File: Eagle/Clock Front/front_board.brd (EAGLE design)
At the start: 9 parts

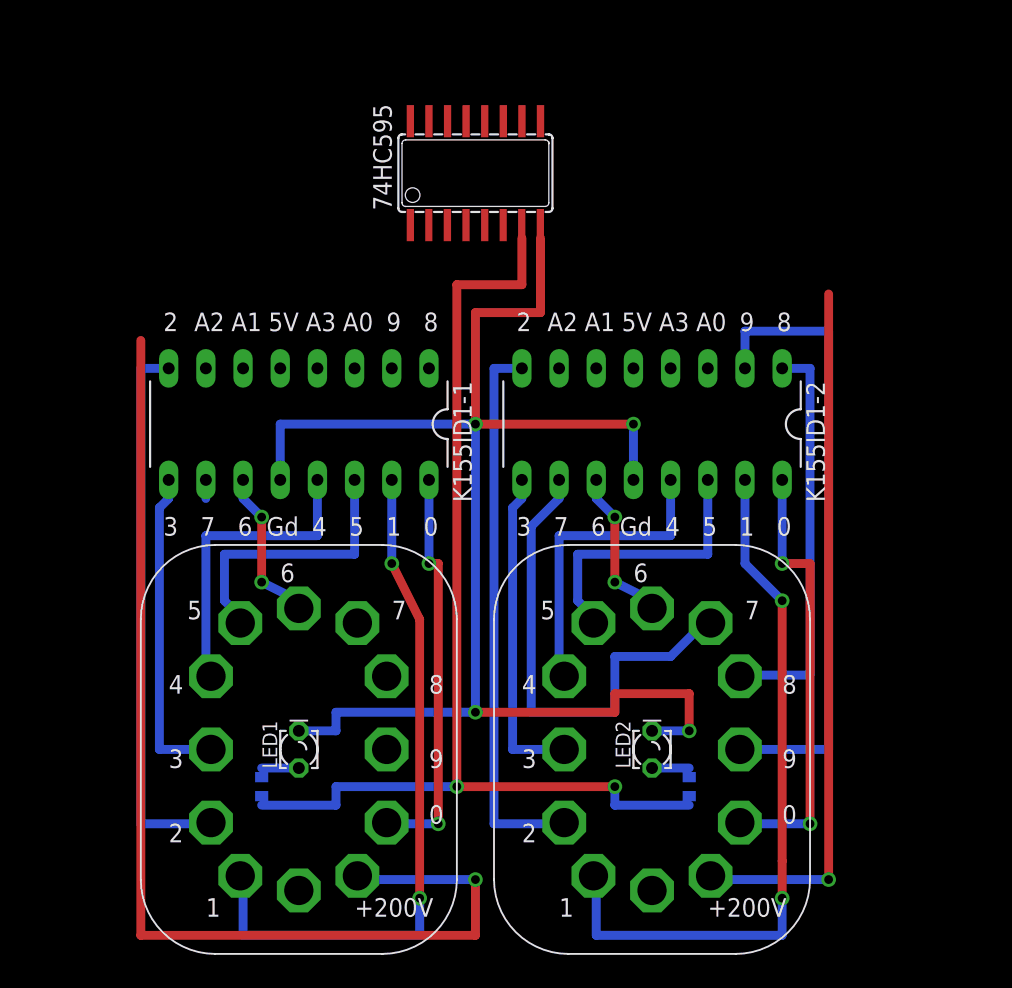
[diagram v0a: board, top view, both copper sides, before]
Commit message: Обновление печатной платы для цоколей
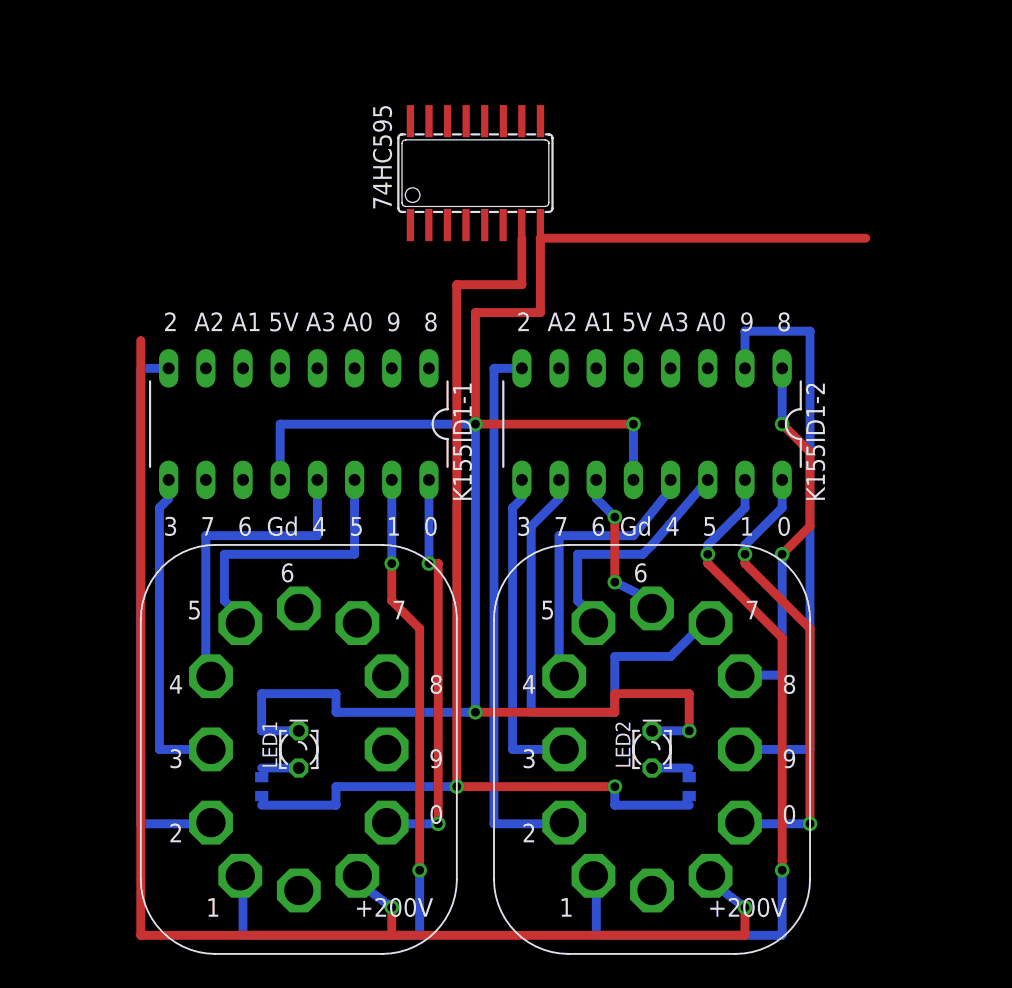
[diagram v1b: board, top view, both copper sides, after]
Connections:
- removed net S$20: K155ID1-1.11
- removed net S$9: K155ID1-1.10
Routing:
- net +200V1: track 75.6 -> 0.00 mm, vias 1 -> 0
- net +200V: track 48.3 -> 92.1 mm, vias 1 -> 2
- net GND: track 102.9 -> 132.7 mm
- net S$20: track 10.4 -> 0.00 mm, vias 2 -> 0
- net S$7: track 18.9 -> 16.2 mm
- net S$2: track 42.5 -> 40.0 mm
- net S$1: track 27.3 -> 25.1 mm, vias 0 -> 2
- net S$12: track 27.1 -> 29.2 mm
- net S$6: track 21.0 -> 19.3 mm
- net S$9: track 1.27 -> 0.00 mm
- net S$3: track 29.8 -> 30.8 mm
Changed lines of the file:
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@@
 <signals>
 <signal name="S$1">
-<wire x1="18.415" y1="-7.62" x2="22.86" y2="-7.62" width="0.6096" layer="16"/>
-<wire x1="22.86" y1="-7.62" x2="22.86" y2="13.335" width="0.6096" layer="16"/>
+<wire x1="18.415" y1="-7.62" x2="20.955" y2="-7.62" width="0.6096" layer="16"/>
+<wire x1="20.955" y1="-7.62" x2="20.955" y2="0.635" width="0.6096" layer="16"/>
+<wire x1="20.955" y1="0.635" x2="22.86" y2="2.54" width="0.6096" layer="1"/>
+<wire x1="22.86" y1="2.54" x2="22.86" y2="7.62" width="0.6096" layer="1"/>
+<wire x1="22.86" y1="7.62" x2="20.955" y2="9.525" width="0.6096" layer="1"/>
 <contactref element="K155ID1-2" pad="1"/>
-<wire x1="22.86" y1="13.335" x2="20.955" y2="13.335" width="0.6096" layer="16"/>
+<wire x1="20.955" y1="9.525" x2="20.955" y2="13.335" width="0.6096" layer="16"/>
+<via x="20.955" y="0.635" extent="1-16" drill="0.6" shape="square"/>
+<via x="20.955" y="9.525" extent="1-16" drill="0.6" shape="square"/>
 </signal>
 <signal name="S$2">
-<wire x1="18.415" y1="-12.7" x2="24.13" y2="-12.7" width="0.6096" layer="16"/>
-<wire x1="24.13" y1="-12.7" x2="24.13" y2="15.875" width="0.6096" layer="16"/>
-<wire x1="24.13" y1="15.875" x2="18.415" y2="15.875" width="0.6096" layer="16"/>
+<wire x1="18.415" y1="-12.7" x2="22.86" y2="-12.7" width="0.6096" layer="16"/>
+<wire x1="22.86" y1="-12.7" x2="22.86" y2="15.875" width="0.6096" layer="16"/>
+<wire x1="22.86" y1="15.875" x2="18.415" y2="15.875" width="0.6096" layer="16"/>
 <contactref element="K155ID1-2" pad="2"/>
 <wire x1="18.415" y1="15.875" x2="18.415" y2="13.335" width="0.6096" layer="16"/>
@@
 <signal name="S$3">
 <wire x1="18.415" y1="-17.78" x2="22.86" y2="-17.78" width="0.6096" layer="16"/>
-<wire x1="22.86" y1="-17.78" x2="22.86" y2="0" width="0.6096" layer="1"/>
-<wire x1="22.86" y1="0" x2="20.955" y2="0" width="0.6096" layer="1"/>
+<wire x1="22.86" y1="-17.78" x2="22.86" y2="-4.445" width="0.6096" layer="1"/>
+<wire x1="22.86" y1="-4.445" x2="18.415" y2="0" width="0.6096" layer="1"/>
+<wire x1="18.415" y1="0" x2="18.415" y2="0.635" width="0.6096" layer="1"/>
 <contactref element="K155ID1-2" pad="16"/>
-<wire x1="20.955" y1="0" x2="20.955" y2="5.715" width="0.6096" layer="16"/>
-<via x="20.955" y="0" extent="1-16" drill="0.6" shape="square"/>
+<wire x1="18.415" y1="0.635" x2="18.415" y2="1.27" width="0.6096" layer="16"/>
+<wire x1="18.415" y1="1.27" x2="20.955" y2="3.81" width="0.6096" layer="16"/>
+<wire x1="20.955" y1="3.81" x2="20.955" y2="5.715" width="0.6096" layer="16"/>
+<via x="18.415" y="0.635" extent="1-16" drill="0.6" shape="square"/>
 <via x="22.86" y="-17.78" extent="1-16" drill="0.6" shape="square"/>
 </signal>
@@
 <signal name="S$6">
 <wire x1="5.715" y1="-7.62" x2="5.715" y2="1.905" width="0.6096" layer="16"/>
-<wire x1="5.715" y1="1.905" x2="13.335" y2="1.905" width="0.6096" layer="16"/>
+<wire x1="5.715" y1="1.905" x2="10.795" y2="1.905" width="0.6096" layer="16"/>
 <contactref element="K155ID1-2" pad="13"/>
-<wire x1="13.335" y1="1.905" x2="13.335" y2="5.715" width="0.6096" layer="16"/>
+<wire x1="10.795" y1="1.905" x2="13.335" y2="5.08" width="0.6096" layer="16"/>
+<wire x1="13.335" y1="5.08" x2="13.335" y2="5.715" width="0.6096" layer="16"/>
 </signal>
 <signal name="S$7">
 <wire x1="8.255" y1="-3.81" x2="6.985" y2="-2.54" width="0.6096" layer="16"/>
 <wire x1="6.985" y1="-2.54" x2="6.985" y2="0.635" width="0.6096" layer="16"/>
-<wire x1="6.985" y1="0.635" x2="15.875" y2="0.635" width="0.6096" layer="16"/>
+<wire x1="6.985" y1="0.635" x2="11.43" y2="0.635" width="0.6096" layer="16"/>
 <contactref element="K155ID1-2" pad="14"/>
-<wire x1="15.875" y1="0.635" x2="15.875" y2="5.715" width="0.6096" layer="16"/>
+<wire x1="11.43" y1="0.635" x2="12.065" y2="1.27" width="0.6096" layer="16"/>
+<wire x1="12.065" y1="1.27" x2="15.875" y2="5.715" width="0.6096" layer="16"/>
 </signal>
 <signal name="S$8">
@@
 </signal>
 <signal name="S$13">
-<wire x1="20.955" y1="-22.86" x2="20.955" y2="-20.32" width="0.6096" layer="1"/>
+<wire x1="20.955" y1="-20.955" x2="20.955" y2="-20.32" width="0.6096" layer="1"/>
 <wire x1="8.255" y1="-21.59" x2="8.255" y2="-25.4" width="0.6096" layer="16"/>
 <wire x1="8.255" y1="-25.4" x2="20.955" y2="-25.4" width="0.6096" layer="16"/>
-<wire x1="20.955" y1="-25.4" x2="20.955" y2="-22.86" width="0.6096" layer="16"/>
-<via x="20.955" y="-22.86" extent="1-16" drill="0.6" shape="square"/>
+<wire x1="20.955" y1="-25.4" x2="20.955" y2="-20.955" width="0.6096" layer="16"/>
+<via x="20.955" y="-20.955" extent="1-16" drill="0.6" shape="square"/>
 </signal>
 <signal name="S$12">
-<wire x1="20.955" y1="-20.32" x2="20.955" y2="-2.54" width="0.6096" layer="1"/>
-<wire x1="20.955" y1="-2.54" x2="18.415" y2="0" width="0.6096" layer="16"/>
+<wire x1="20.955" y1="-20.32" x2="20.955" y2="-5.08" width="0.6096" layer="1"/>
+<wire x1="20.955" y1="-5.08" x2="15.875" y2="0" width="0.6096" layer="1"/>
+<wire x1="15.875" y1="0" x2="15.875" y2="0.635" width="0.6096" layer="1"/>
 <contactref element="K155ID1-2" pad="15"/>
-<wire x1="18.415" y1="0" x2="18.415" y2="5.715" width="0.6096" layer="16"/>
-<via x="20.955" y="-2.54" extent="1-16" drill="0.6" shape="square"/>
+<wire x1="15.875" y1="0.635" x2="15.875" y2="1.27" width="0.6096" layer="16"/>
+<wire x1="15.875" y1="1.27" x2="18.415" y2="3.81" width="0.6096" layer="16"/>
+<wire x1="18.415" y1="3.81" x2="18.415" y2="5.715" width="0.6096" layer="16"/>
+<via x="15.875" y="0.635" extent="1-16" drill="0.6" shape="square"/>
 </signal>
 <signal name="S$11">
@@
 </signal>
 <signal name="+200V">
-<wire x1="15.875" y1="-21.59" x2="24.13" y2="-21.59" width="0.6096" layer="16"/>
-<via x="24.13" y="-21.59" extent="1-16" drill="0.6" shape="square"/>
-<wire x1="24.13" y1="-21.59" x2="24.13" y2="18.415" width="0.6096" layer="1"/>
+<wire x1="15.875" y1="-21.59" x2="18.415" y2="-23.495" width="0.6096" layer="16"/>
+<via x="18.415" y="-23.495" extent="1-16" drill="0.6" shape="square"/>
+<wire x1="18.415" y1="-23.495" x2="18.415" y2="-25.4" width="0.6096" layer="1"/>
+<wire x1="-8.255" y1="-21.59" x2="-5.715" y2="-23.495" width="0.6096" layer="16"/>
+<via x="-5.715" y="-23.495" extent="1-16" drill="0.6" shape="square"/>
+<wire x1="-5.715" y1="-23.495" x2="-5.715" y2="-25.4" width="0.6096" layer="1"/>
+<wire x1="-5.715" y1="-25.4" x2="-22.86" y2="-25.4" width="0.6096" layer="1"/>
+<wire x1="-22.86" y1="-25.4" x2="-22.86" y2="15.24" width="0.6096" layer="1"/>
+<wire x1="18.415" y1="-25.4" x2="-5.715" y2="-25.4" width="0.6096" layer="1"/>
 </signal>
 <signal name="S$14">
@@
 <wire x1="-8.255" y1="0.635" x2="-8.255" y2="5.715" width="0.6096" layer="16"/>
 </signal>
-<signal name="S$9">
-<contactref element="K155ID1-1" pad="10"/>
-<wire x1="-18.415" y1="4.445" x2="-18.415" y2="5.715" width="0.6096" layer="16"/>
-</signal>
-<signal name="S$20">
-<wire x1="-12.065" y1="-2.54" x2="-14.605" y2="-1.27" width="0.6096" layer="16"/>
-<contactref element="K155ID1-1" pad="11"/>
-<wire x1="-15.875" y1="4.445" x2="-15.875" y2="5.715" width="0.6096" layer="16"/>
-<wire x1="-14.605" y1="-1.27" x2="-14.605" y2="3.175" width="0.6096" layer="1"/>
-<wire x1="-14.605" y1="3.175" x2="-15.875" y2="4.445" width="0.6096" layer="16"/>
-<via x="-14.605" y="-1.27" extent="1-16" drill="0.6" shape="square"/>
-<via x="-14.605" y="3.175" extent="1-16" drill="0.6" shape="square"/>
-</signal>
 <signal name="S$22">
-<wire x1="-3.81" y1="-22.86" x2="-3.81" y2="-3.81" width="0.6096" layer="1"/>
-<wire x1="-3.81" y1="-3.81" x2="-5.715" y2="0" width="0.6096" layer="1"/>
+<wire x1="-3.81" y1="-20.955" x2="-3.81" y2="-4.445" width="0.6096" layer="1"/>
+<wire x1="-3.81" y1="-4.445" x2="-5.715" y2="-2.54" width="0.6096" layer="1"/>
+<wire x1="-5.715" y1="-2.54" x2="-5.715" y2="0" width="0.6096" layer="1"/>
 <contactref element="K155ID1-1" pad="15"/>
 <wire x1="-5.715" y1="0" x2="-5.715" y2="5.715" width="0.6096" layer="16"/>
@@
 <wire x1="-15.875" y1="-21.59" x2="-15.875" y2="-25.4" width="0.6096" layer="16"/>
 <wire x1="-15.875" y1="-25.4" x2="-3.81" y2="-25.4" width="0.6096" layer="16"/>
-<wire x1="-3.81" y1="-25.4" x2="-3.81" y2="-22.86" width="0.6096" layer="16"/>
-<via x="-3.81" y="-22.86" extent="1-16" drill="0.6" shape="square"/>
+<wire x1="-3.81" y1="-25.4" x2="-3.81" y2="-20.955" width="0.6096" layer="16"/>
+<via x="-3.81" y="-20.955" extent="1-16" drill="0.6" shape="square"/>
 </signal>
 <signal name="GND1">
 <wire x1="-22.86" y1="-15.24" x2="-22.86" y2="9.525" width="0" layer="19" extent="1-16"/>
 <wire x1="-22.86" y1="-15.24" x2="-24.13" y2="-15.24" width="0" layer="19" extent="1-16"/>
-</signal>
-<signal name="+200V1">
-<wire x1="-8.255" y1="-21.59" x2="0" y2="-21.59" width="0.6096" layer="16"/>
-<via x="0" y="-21.59" extent="1-16" drill="0.6" shape="square"/>
-<wire x1="0" y1="-21.59" x2="0" y2="-25.4" width="0.6096" layer="1"/>
-<wire x1="0" y1="-25.4" x2="-22.86" y2="-25.4" width="0.6096" layer="1"/>
-<wire x1="-22.86" y1="-25.4" x2="-22.86" y2="15.24" width="0.6096" layer="1"/>
 </signal>
 <signal name="S$19">
@@
 <wire x1="-13.335" y1="9.525" x2="0" y2="9.525" width="0.6096" layer="16"/>
 <contactref element="LED1" pad="K"/>
-<wire x1="-12.065" y1="-11.43" x2="-9.525" y2="-11.43" width="0.6096" layer="16"/>
-<wire x1="-9.525" y1="-11.43" x2="-9.525" y2="-10.16" width="0.6096" layer="16"/>
+<wire x1="-12.065" y1="-11.43" x2="-14.605" y2="-11.43" width="0.6096" layer="16"/>
+<wire x1="-14.605" y1="-11.43" x2="-14.605" y2="-8.89" width="0.6096" layer="16"/>
+<wire x1="-14.605" y1="-8.89" x2="-9.525" y2="-8.89" width="0.6096" layer="16"/>
+<wire x1="-9.525" y1="-8.89" x2="-9.525" y2="-10.16" width="0.6096" layer="16"/>
 <wire x1="-9.525" y1="-10.16" x2="0" y2="-10.16" width="0.6096" layer="16"/>
 <via x="0" y="-10.16" extent="1-16" drill="0.6" shape="square"/>
@@
 <via x="0" y="9.525" extent="1-16" drill="0.6" shape="square"/>
 <via x="10.795" y="9.525" extent="1-16" drill="0.6" shape="square"/>
+<wire x1="4.445" y1="22.225" x2="26.67" y2="22.225" width="0.6096" layer="1"/>
 </signal>
 </signals>

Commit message: Обновление печатной платы для цоколей. Полностью разведены К155ИД1
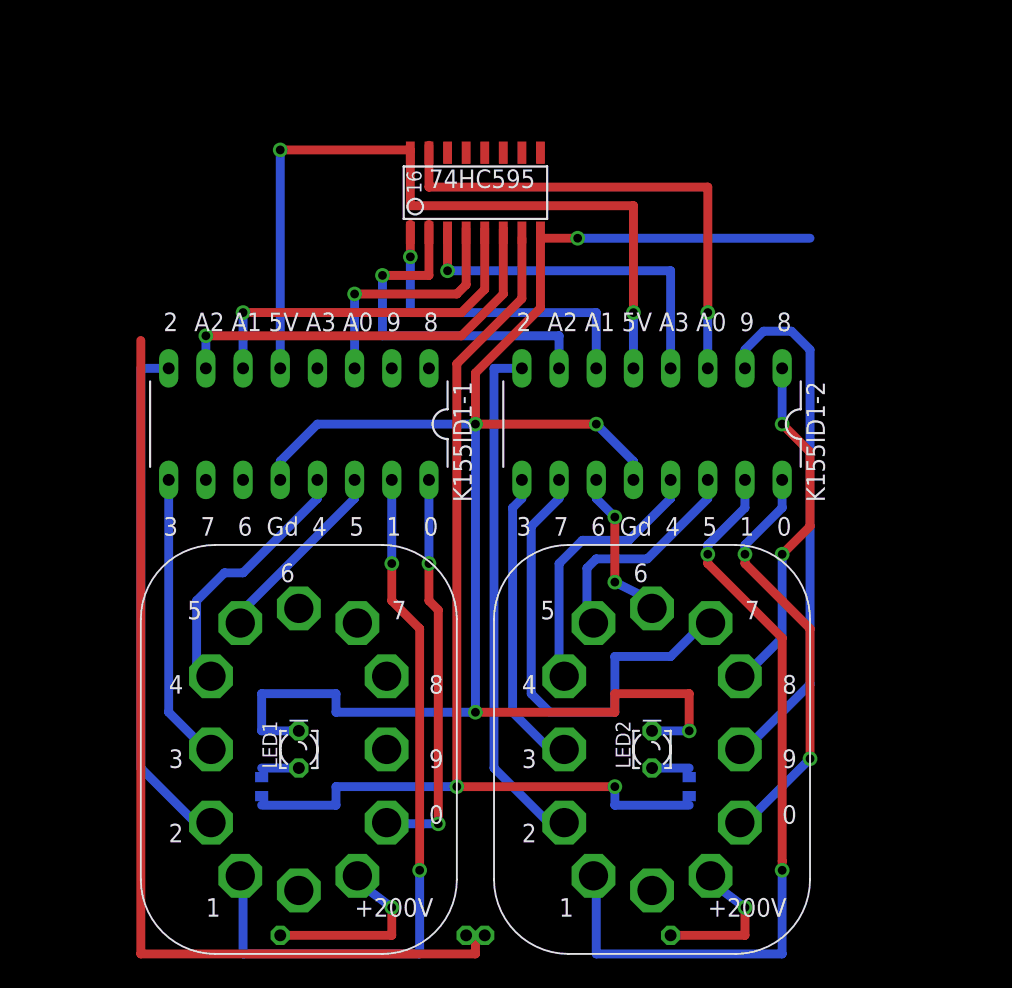
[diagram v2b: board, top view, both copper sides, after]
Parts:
- added E$3, E$4: (no value), rcl:0309/12
- 74HC595: device exar:SOP-16 -> texas:SO-16
- moved 74HC595 1.27 mm to (0.00, 25.4)
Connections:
- new net +200V: E$3.1, E$4.2
- new net +5V: K155ID1-1.5, K155ID1-2.5
- new net S$20: K155ID1-1.6
- new net S$21: K155ID1-1.3
- new net S$23: K155ID1-2.3
- new net S$24: K155ID1-2.4
- new net S$25: K155ID1-2.7
- new net S$26: K155ID1-2.6
- new net S$9: K155ID1-1.7
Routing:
- net +5V: track 0.00 -> 54.0 mm, vias 0 -> 2
- net S$23: track 0.00 -> 34.3 mm, vias 0 -> 1
- net S$9: track 0.00 -> 28.2 mm, vias 0 -> 1
- net S$20: track 0.00 -> 25.1 mm, vias 0 -> 1
- net S$25: track 0.00 -> 25.1 mm, vias 0 -> 1
- net S$24: track 0.00 -> 24.8 mm, vias 0 -> 1
- net +200V: track 92.1 -> 67.3 mm, vias 2 -> 0
- net S$26: track 0.00 -> 22.5 mm, vias 0 -> 1
- net S$21: track 0.00 -> 16.8 mm, vias 0 -> 1
- net +200V_LEFT: track 0.00 -> 12.7 mm, vias 0 -> 1
- net +200V_RIGHT: track 0.00 -> 10.2 mm, vias 0 -> 1
- net GND: track 132.7 -> 123.3 mm, vias 4 -> 5
- net S$18: track 18.9 -> 12.7 mm
- net S$2: track 40.0 -> 35.9 mm
- net S$17: track 21.0 -> 17.8 mm
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
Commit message: Обновление печатной платы для цоколей. Первый вариант полностью готов.
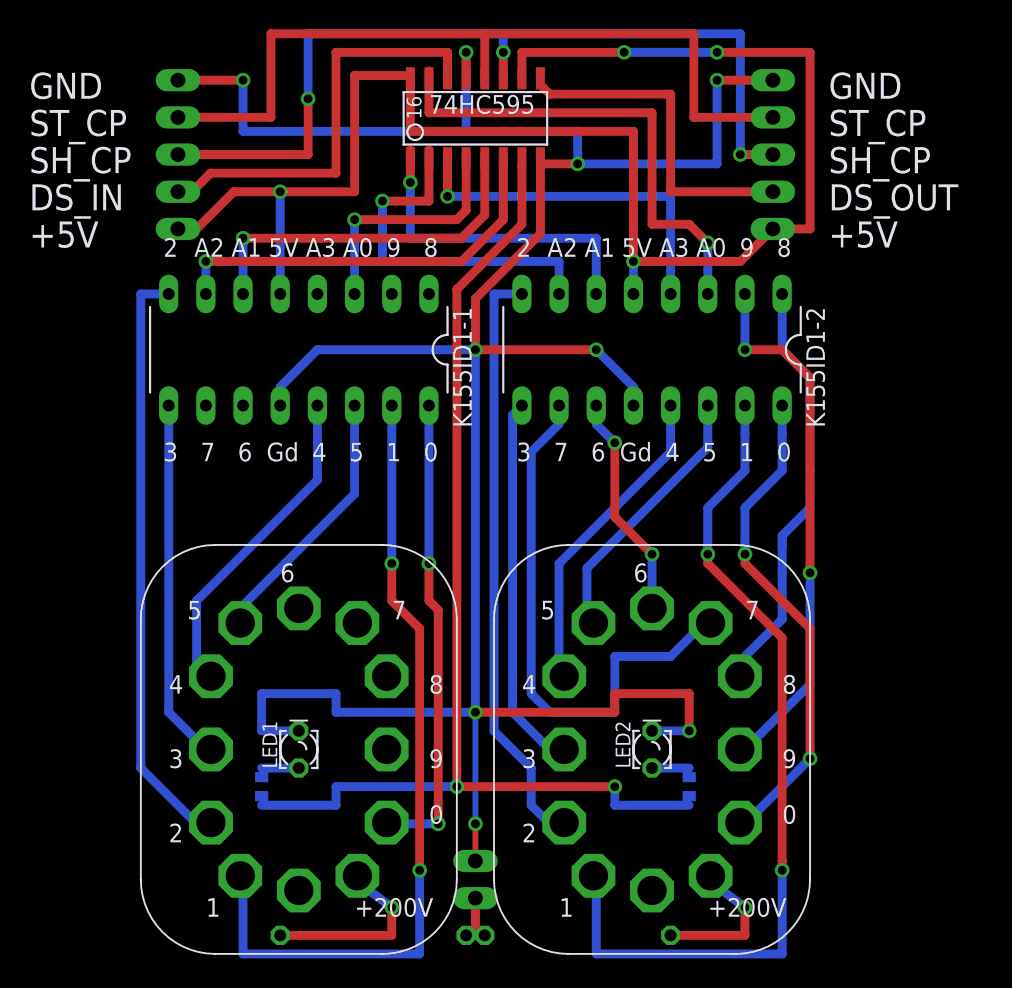
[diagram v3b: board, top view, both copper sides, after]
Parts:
- added 200VCONNECTOR: (no value), pinhead:1X02
- added IN, OUT: (no value), pinhead:1X05
- moved 74HC595 5.08 mm to (0.00, 30.5)
- moved K155ID1-1 5.08 mm to (-12.1, 14.6)
- moved K155ID1-2 5.08 mm to (12.1, 14.6)
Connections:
- new net DATA_IN: IN.2
- new net DATA_OUT: OUT.2
- new net SH_CP: IN.3, OUT.3
- new net ST_CP: IN.4, OUT.4
- net +5V: now also IN.1, OUT.1
- net GND: now also IN.5
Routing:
- net +200V: track 67.3 -> 3.81 mm
- net SH_CP: track 0.00 -> 60.6 mm, vias 0 -> 3
- net GND: track 123.3 -> 182.4 mm, vias 5 -> 9
- net ST_CP: track 0.00 -> 55.6 mm
- net +5V: track 54.0 -> 109.0 mm, vias 2 -> 4
- net DATA_IN: track 0.00 -> 29.1 mm
- net DATA_OUT: track 0.00 -> 22.8 mm
- net S$3: track 28.2 -> 33.3 mm
- net S$18: track 12.7 -> 17.8 mm
- net S$8: track 32.8 -> 37.9 mm
- net S$5: track 35.2 -> 40.3 mm
- net S$4: track 20.4 -> 25.4 mm
- net S$22: track 50.3 -> 55.4 mm
- net S$16: track 35.2 -> 40.3 mm
- net S$15: track 19.5 -> 24.5 mm
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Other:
- board text added: "+5V"
- board text added: "DS_IN"
- board text added: "DS_OUT"
- board text added: "GND"
- board text added: "SH_CP"
- board text added: "ST_CP"
